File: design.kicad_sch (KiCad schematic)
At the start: 67 parts, among them J1 Pins, J2 Programming, J3 HRO_TYPE-C-31-M-12, Q1 Q_PMOS_GSD, SW1 Control, SW2 EN, SW3 IO0, U1 MCP1700-3302E_SOT23, U2 TCK127BG, U3 AP3015, U4 ESP32-C3-WROOM-02-N4, U5 TTP223, U6 TTP223

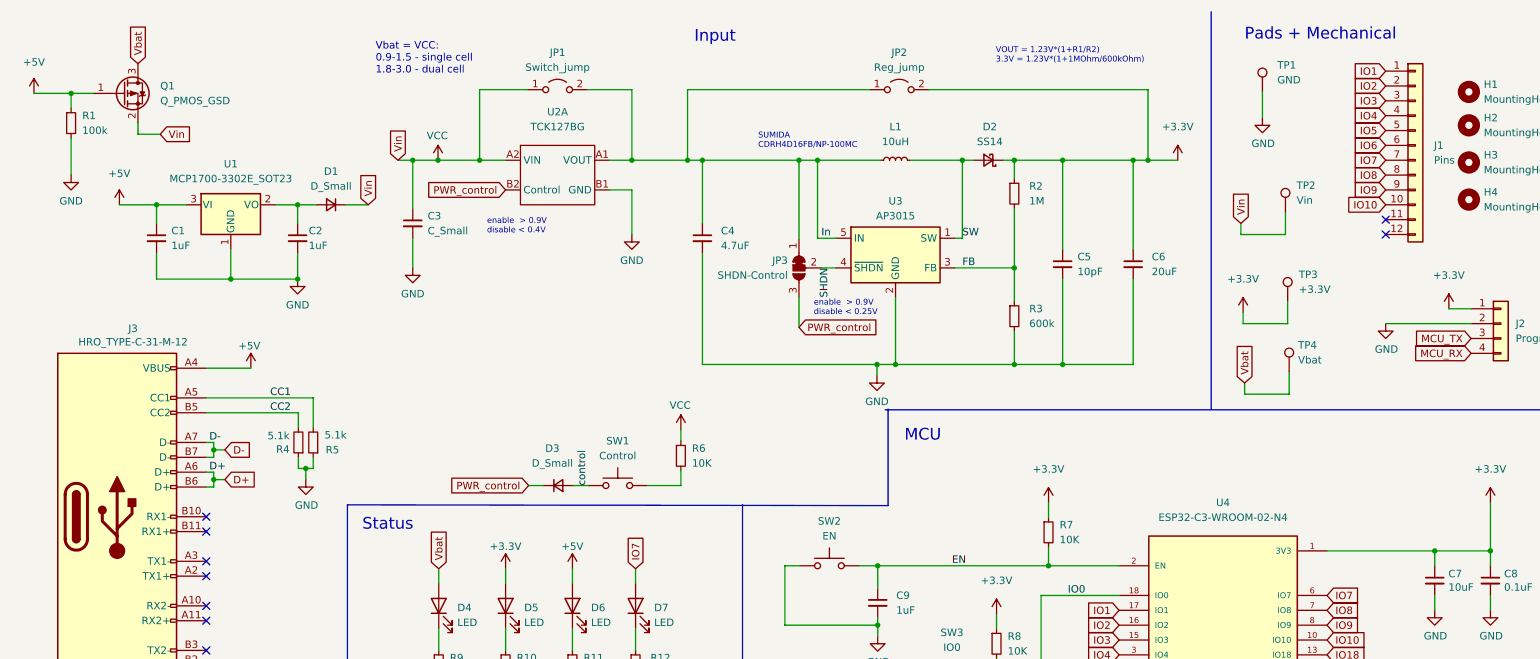
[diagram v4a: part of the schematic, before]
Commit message: rounded corners + mounting holes with copper
closes #7
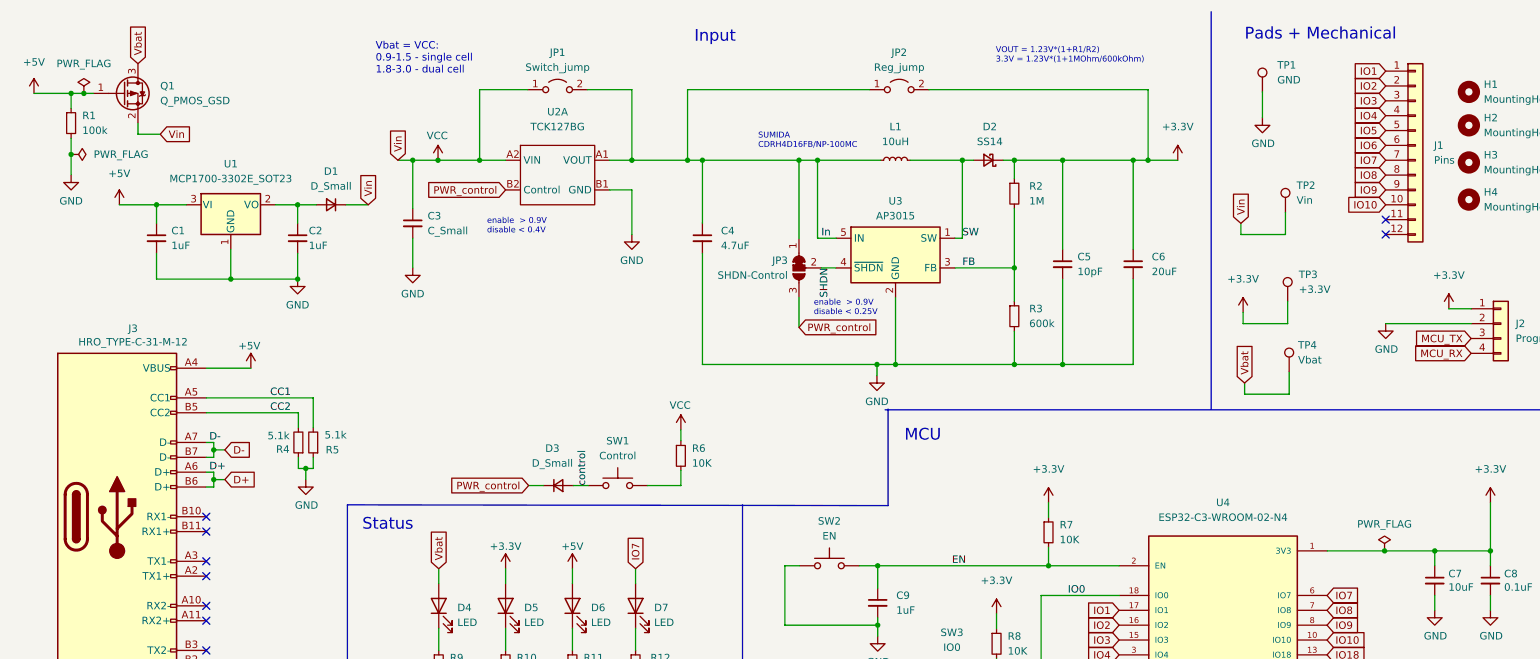
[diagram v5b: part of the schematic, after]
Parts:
- H1, H2, H3, H4: footprint MountingHole:MountingHole_3.2mm_M3 -> MountingHole:MountingHole_3.2mm_M3_Pad_Via
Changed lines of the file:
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@@
   (junction (at 48.895 57.15) (diameter 0) (color 0 0 0 0)
   )
+  (junction (at 246.1768 103.632) (diameter 0) (color 0 0 0 0)
+  )
   (junction (at 191.135 36.83) (diameter 0) (color 0 0 0 0)
   )
@@
   (junction (at 205.74 36.83) (diameter 0) (color 0 0 0 0)
   )
+  (junction (at 21.59 35.8394) (diameter 0) (color 0 0 0 0)
+  )
+  (junction (at 23.7744 25.4) (diameter 0) (color 0 0 0 0)
+  )
   (junction (at 129.54 36.83) (diameter 0) (color 0 0 0 0)
   )
@@
     (stroke (width 0) (type default) (color 0 0 0 0))
   )
-  (wire (pts (xy 44.704 72.39) (xy 52.324 72.39))
-    (stroke (width 0) (type default) (color 0 0 0 0))
-  )
   (wire (pts (xy 60.452 89.535) (xy 61.722 89.535))
     (stroke (width 0) (type default) (color 0 0 0 0))
@@
     (stroke (width 0) (type default) (color 0 0 0 0))
   )
+  (wire (pts (xy 44.704 72.39) (xy 52.324 72.39))
+    (stroke (width 0) (type default) (color 0 0 0 0))
+  )
   (wire (pts (xy 191.135 36.83) (xy 191.135 52.07))
     (stroke (width 0) (type default) (color 0 0 0 0))
@@
     (stroke (width 0) (type default) (color 0 0 0 0))
   )
+  (wire (pts (xy 15.24 25.4) (xy 21.59 25.4))
+    (stroke (width 0) (type default) (color 0 0 0 0))
+  )
   (wire (pts (xy 159.512 115.062) (xy 159.512 116.332))
     (stroke (width 0) (type default) (color 0 0 0 0))
@@
     (stroke (width 0) (type default) (color 0 0 0 0))
   )
-  (wire (pts (xy 236.347 103.632) (xy 254.762 103.632))
+  (wire (pts (xy 236.347 103.632) (xy 246.1768 103.632))
     (stroke (width 0) (type default) (color 0 0 0 0))
   )
@@
     (stroke (width 0) (type default) (color 0 0 0 0))
   )
-  (wire (pts (xy 15.24 25.4) (xy 21.59 25.4))
-    (stroke (width 0) (type default) (color 0 0 0 0))
-  )
   (wire (pts (xy 40.767 158.877) (xy 42.037 158.877))
     (stroke (width 0) (type default) (color 0 0 0 0))
@@
     (stroke (width 0) (type default) (color 0 0 0 0))
   )
-  (wire (pts (xy 21.59 25.4) (xy 25.4 25.4))
+  (wire (pts (xy 21.59 25.4) (xy 23.7744 25.4))
     (stroke (width 0) (type default) (color 0 0 0 0))
   )
@@
     (stroke (width 0) (type default) (color 0 0 0 0))
   )
-  (wire (pts (xy 80.01 36.83) (xy 84.328 36.83))
-    (stroke (width 0) (type default) (color 0 0 0 0))
-  )
   (wire (pts (xy 107.315 106.68) (xy 107.315 109.22))
     (stroke (width 0) (type default) (color 0 0 0 0))
@@
     (stroke (width 0) (type default) (color 0 0 0 0))
   )
+  (wire (pts (xy 21.59 35.8394) (xy 21.59 39.37))
+    (stroke (width 0) (type default) (color 0 0 0 0))
+  )
   (wire (pts (xy 129.54 36.83) (xy 146.05 36.83))
     (stroke (width 0) (type default) (color 0 0 0 0))
@@
     (stroke (width 0) (type default) (color 0 0 0 0))
   )
-  (wire (pts (xy 21.59 33.02) (xy 21.59 39.37))
+  (wire (pts (xy 21.59 33.02) (xy 21.59 35.8394))
     (stroke (width 0) (type default) (color 0 0 0 0))
   )
@@
     (stroke (width 0) (type default) (color 0 0 0 0))
   )
+  (wire (pts (xy 80.01 36.83) (xy 84.328 36.83))
+    (stroke (width 0) (type default) (color 0 0 0 0))
+  )
   (wire (pts (xy 83.82 166.116) (xy 83.82 168.656))
     (stroke (width 0) (type default) (color 0 0 0 0))
@@
     (stroke (width 0) (type default) (color 0 0 0 0))
   )
+  (wire (pts (xy 246.1768 103.632) (xy 254.762 103.632))
+    (stroke (width 0) (type default) (color 0 0 0 0))
+  )
+  (wire (pts (xy 23.7744 25.4) (xy 25.4 25.4))
+    (stroke (width 0) (type default) (color 0 0 0 0))
+  )
   (text "enable  > 0.9V\ndisable < 0.25V" (at 148.59 63.5 0)
     (effects (font (size 1 1)) (justify left bottom))
@@
     (pin "2")
   )
+  (symbol (lib_id "power:PWR_FLAG") (at 246.1768 103.632 0) (unit 1)
+    (in_bom yes) (on_board yes) (fields_autoplaced)
+    (property "Reference" "#FLG0103" (id 0) (at 246.1768 101.727 0)
+      (effects (font (size 1.27 1.27)) hide)
+    )
+    (property "Value" "PWR_FLAG" (id 1) (at 246.1768 99.06 0))
+    (property "Footprint" "" (id 2) (at 246.1768 103.632 0)
+      (effects (font (size 1.27 1.27)) hide)
+    )
+    (property "Datasheet" "~" (id 3) (at 246.1768 103.632 0)
+      (effects (font (size 1.27 1.27)) hide)
+    )
+    (pin "1")
+  )
   (symbol (lib_id "Device:R_Small") (at 182.88 63.5 0) (unit 1)
     (in_bom yes) (on_board yes) (fields_autoplaced)
@@
       (effects (font (size 1.27 1.27)) (justify left))
     )
-    (property "Footprint" "MountingHole:MountingHole_3.2mm_M3" (id 2) (at 260.604 43.561 0)
+    (property "Footprint" "MountingHole:MountingHole_3.2mm_M3_Pad_Via" (id 2) (at 260.604 43.561 0)
       (effects (font (size 1.27 1.27)) hide)
     )
@@
       (effects (font (size 1.27 1.27)) (justify left))
     )
-    (property "Footprint" "MountingHole:MountingHole_3.2mm_M3" (id 2) (at 260.604 30.861 0)
+    (property "Footprint" "MountingHole:MountingHole_3.2mm_M3_Pad_Via" (id 2) (at 260.604 30.861 0)
       (effects (font (size 1.27 1.27)) hide)
     )
@@
       (effects (font (size 1.27 1.27)) (justify left))
     )
-    (property "Footprint" "MountingHole:MountingHole_3.2mm_M3" (id 2) (at 260.604 25.146 0)
+    (property "Footprint" "MountingHole:MountingHole_3.2mm_M3_Pad_Via" (id 2) (at 260.604 25.146 0)
       (effects (font (size 1.27 1.27)) hide)
     )
@@
       (effects (font (size 1.27 1.27)) (justify left))
     )
-    (property "Footprint" "MountingHole:MountingHole_3.2mm_M3" (id 2) (at 260.604 37.211 0)
+    (property "Footprint" "MountingHole:MountingHole_3.2mm_M3_Pad_Via" (id 2) (at 260.604 37.211 0)
       (effects (font (size 1.27 1.27)) hide)
     )
@@
     )
   )
+  (symbol (lib_id "power:PWR_FLAG") (at 23.7744 25.4 0) (unit 1)
+    (in_bom yes) (on_board yes) (fields_autoplaced)
+    (property "Reference" "#FLG0102" (id 0) (at 23.7744 23.495 0)
+      (effects (font (size 1.27 1.27)) hide)
+    )
+    (property "Value" "PWR_FLAG" (id 1) (at 23.7744 20.32 0))
+    (property "Footprint" "" (id 2) (at 23.7744 25.4 0)
+      (effects (font (size 1.27 1.27)) hide)
+    )
+    (property "Datasheet" "~" (id 3) (at 23.7744 25.4 0)
+      (effects (font (size 1.27 1.27)) hide)
+    )
+    (pin "1")
+  )
+  (symbol (lib_id "power:PWR_FLAG") (at 21.59 35.8394 270) (unit 1)
+    (in_bom yes) (on_board yes) (fields_autoplaced)
+    (property "Reference" "#FLG0101" (id 0) (at 23.495 35.8394 0)
+      (effects (font (size 1.27 1.27)) hide)
+    )
+    (property "Value" "PWR_FLAG" (id 1) (at 25.4508 35.8393 90)
+      (effects (font (size 1.27 1.27)) (justify left))
+    )
+    (property "Footprint" "" (id 2) (at 21.59 35.8394 0)
+      (effects (font (size 1.27 1.27)) hide)
+    )
+    (property "Datasheet" "~" (id 3) (at 21.59 35.8394 0)
+      (effects (font (size 1.27 1.27)) hide)
+    )
+    (pin "1")
+  )
   (symbol (lib_id "Device:C_Small") (at 129.54 50.165 0) (unit 1)
     (in_bom yes) (on_board yes) (fields_autoplaced)
@@
   )
   (symbol_instances
+    (path "/ee247672-ce43-412c-bcbc-60fb27fe4734"
+      (reference "#FLG0101") (unit 1) (value "PWR_FLAG") (footprint "")
+    )
+    (path "/ed24a532-8c5f-4564-9824-1d08d6eedd2e"
+      (reference "#FLG0102") (unit 1) (value "PWR_FLAG") (footprint "")
+    )
+    (path "/19186209-ccaa-43fb-8647-23a278c470e4"
+      (reference "#FLG0103") (unit 1) (value "PWR_FLAG") (footprint "")
+    )
     (path "/d5b22071-197e-41e9-9118-29e2ca59b3b2"
       (reference "#PWR01") (unit 1) (value "+5V") (footprint "")
@@
     )
     (path "/bb16c4c5-bde4-441d-9936-404e59abe7f3"
-      (reference "H1") (unit 1) (value "MountingHole") (footprint "MountingHole:MountingHole_3.2mm_M3")
+      (reference "H1") (unit 1) (value "MountingHole") (footprint "MountingHole:MountingHole_3.2mm_M3_Pad_Via")
     )
     (path "/2dce60a0-35a4-4371-a7d3-616464e52760"
-      (reference "H2") (unit 1) (value "MountingHole") (footprint "MountingHole:MountingHole_3.2mm_M3")
+      (reference "H2") (unit 1) (value "MountingHole") (footprint "MountingHole:MountingHole_3.2mm_M3_Pad_Via")
     )
     (path "/ec3b2cbe-9ceb-4c8a-9613-6bcc19fddb36"
-      (reference "H3") (unit 1) (value "MountingHole") (footprint "MountingHole:MountingHole_3.2mm_M3")
+      (reference "H3") (unit 1) (value "MountingHole") (footprint "MountingHole:MountingHole_3.2mm_M3_Pad_Via")
     )
     (path "/1c3c3584-5a0b-44a9-9a7b-076e5ff044b6"
-      (reference "H4") (unit 1) (value "MountingHole") (footprint "MountingHole:MountingHole_3.2mm_M3")
+      (reference "H4") (unit 1) (value "MountingHole") (footprint "MountingHole:MountingHole_3.2mm_M3_Pad_Via")
     )
     (path "/718c6759-35fc-4398-867b-6d8d18d79b88"

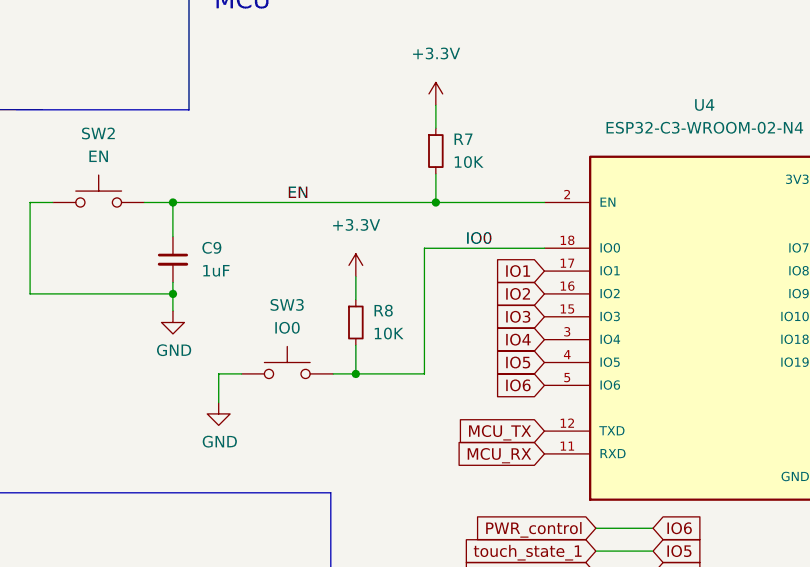
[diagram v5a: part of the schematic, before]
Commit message: pin IO9 connect to push button instead of IO0 (#11)
* pin IO9 connect to push button instead of IO0
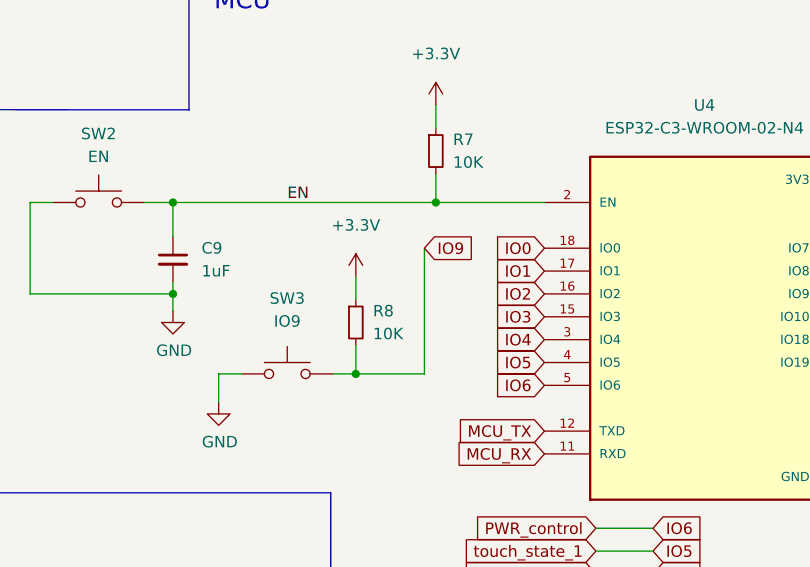
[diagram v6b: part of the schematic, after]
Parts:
- SW3: value IO0 -> IO9
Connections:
- net IO0: no longer R8.2, SW3.2
- net IO9: now also R8.2, SW3.2
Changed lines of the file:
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@@
-    (stroke (width 0) (type default) (color 0 0 0 0))
-  )
-  (wire (pts (xy 200.787 111.252) (xy 187.452 111.252))
     (stroke (width 0) (type default) (color 0 0 0 0))
   )
@@
   (label "SHDN" (at 151.384 55.245 270)
     (effects (font (size 1.27 1.27)) (justify right bottom))
-  )
-  (label "IO0" (at 192.024 111.252 0)
-    (effects (font (size 1.27 1.27)) (justify left bottom))
   )
   (label "CC1" (at 55.626 77.47 0)
@@
     )
   )
+  (global_label "IO0" (shape input) (at 200.787 111.252 180) (fields_autoplaced)
+    (effects (font (size 1.27 1.27)) (justify right))
+    (property "Intersheet References" "${INTERSHEET_REFS}" (id 0) (at 195.318 111.1726 0)
+      (effects (font (size 1.27 1.27)) (justify right) hide)
+    )
+  )
   (global_label "touch_point_2" (shape input) (at 141.224 187.452 0) (fields_autoplaced)
     (effects (font (size 1.27 1.27)) (justify left))
@@
     )
   )
+  (global_label "IO9" (shape input) (at 187.452 111.252 0) (fields_autoplaced)
+    (effects (font (size 1.27 1.27)) (justify left))
+    (property "Intersheet References" "${INTERSHEET_REFS}" (id 0) (at 192.921 111.1726 0)
+      (effects (font (size 1.27 1.27)) (justify left) hide)
+    )
+  )
   (global_label "Vbat" (shape input) (at 222.25 74.93 90) (fields_autoplaced)
     (effects (font (size 1.27 1.27)) (justify left))
@@
   (symbol (lib_id "Switch:SW_Push") (at 172.212 125.222 0) (unit 1)
     (in_bom yes) (on_board yes) (fields_autoplaced)
-    (property "Reference" "SW3" (id 0) (at 172.212 117.602 0))
-    (property "Value" "IO0" (id 1) (at 172.212 120.142 0))
+    (property "Reference" "SW3" (id 0) (at 172.212 116.84 0))
+    (property "Value" "IO9" (id 1) (at 172.212 119.38 0))
     (property "Footprint" "Button_Switch_SMD:SW_SPST_EVPBF" (id 2) (at 172.212 120.142 0)
       (effects (font (size 1.27 1.27)) hide)
@@
     )
     (path "/0b565da2-d5e3-46b1-b63b-b204495f7059"
-      (reference "SW3") (unit 1) (value "IO0") (footprint "Button_Switch_SMD:SW_SPST_EVPBF")
+      (reference "SW3") (unit 1) (value "IO9") (footprint "Button_Switch_SMD:SW_SPST_EVPBF")
     )
     (path "/d4d48133-5782-4e5d-9c70-21ee052cf591"

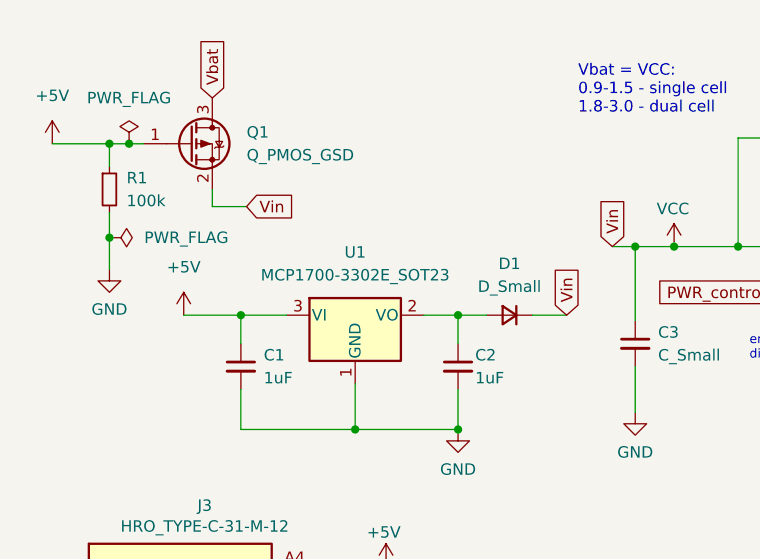
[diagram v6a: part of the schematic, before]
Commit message: use 3.6V regulator
because of voltage drop on Diode
closes #10
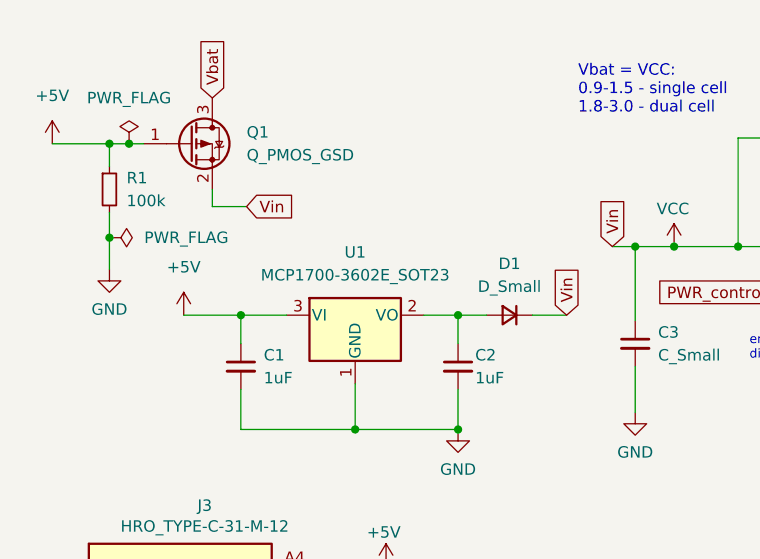
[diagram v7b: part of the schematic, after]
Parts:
- U1: value MCP1700-3302E_SOT23 -> MCP1700-3602E_SOT23
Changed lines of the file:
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@@
     (in_bom yes) (on_board yes)
     (property "Reference" "U1" (id 0) (at 48.895 37.465 0))
-    (property "Value" "MCP1700-3302E_SOT23" (id 1) (at 48.895 40.005 0))
+    (property "Value" "MCP1700-3602E_SOT23" (id 1) (at 48.895 40.005 0))
     (property "Footprint" "Package_TO_SOT_SMD:SOT-23" (id 2) (at 48.895 38.735 0)
       (effects (font (size 1.27 1.27)) hide)
@@
     )
     (path "/8fa72335-445b-41aa-9b88-7ae31dad4a5e"
-      (reference "U1") (unit 1) (value "MCP1700-3302E_SOT23") (footprint "Package_TO_SOT_SMD:SOT-23")
+      (reference "U1") (unit 1) (value "MCP1700-3602E_SOT23") (footprint "Package_TO_SOT_SMD:SOT-23")
     )
     (path "/25ada721-670a-4020-ae0b-77410c4e375a"
